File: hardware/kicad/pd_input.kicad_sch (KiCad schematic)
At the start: 46 parts, among them J1 USB-C USB (Power), J14 noknok_Pico_Socket_P1-20, J15 noknok_Pico_Socket_P21-40, J8 SWD pads, U1 CH32X035G8U6, U4 INA180A2, U5 noknok_ME6203A33M3G

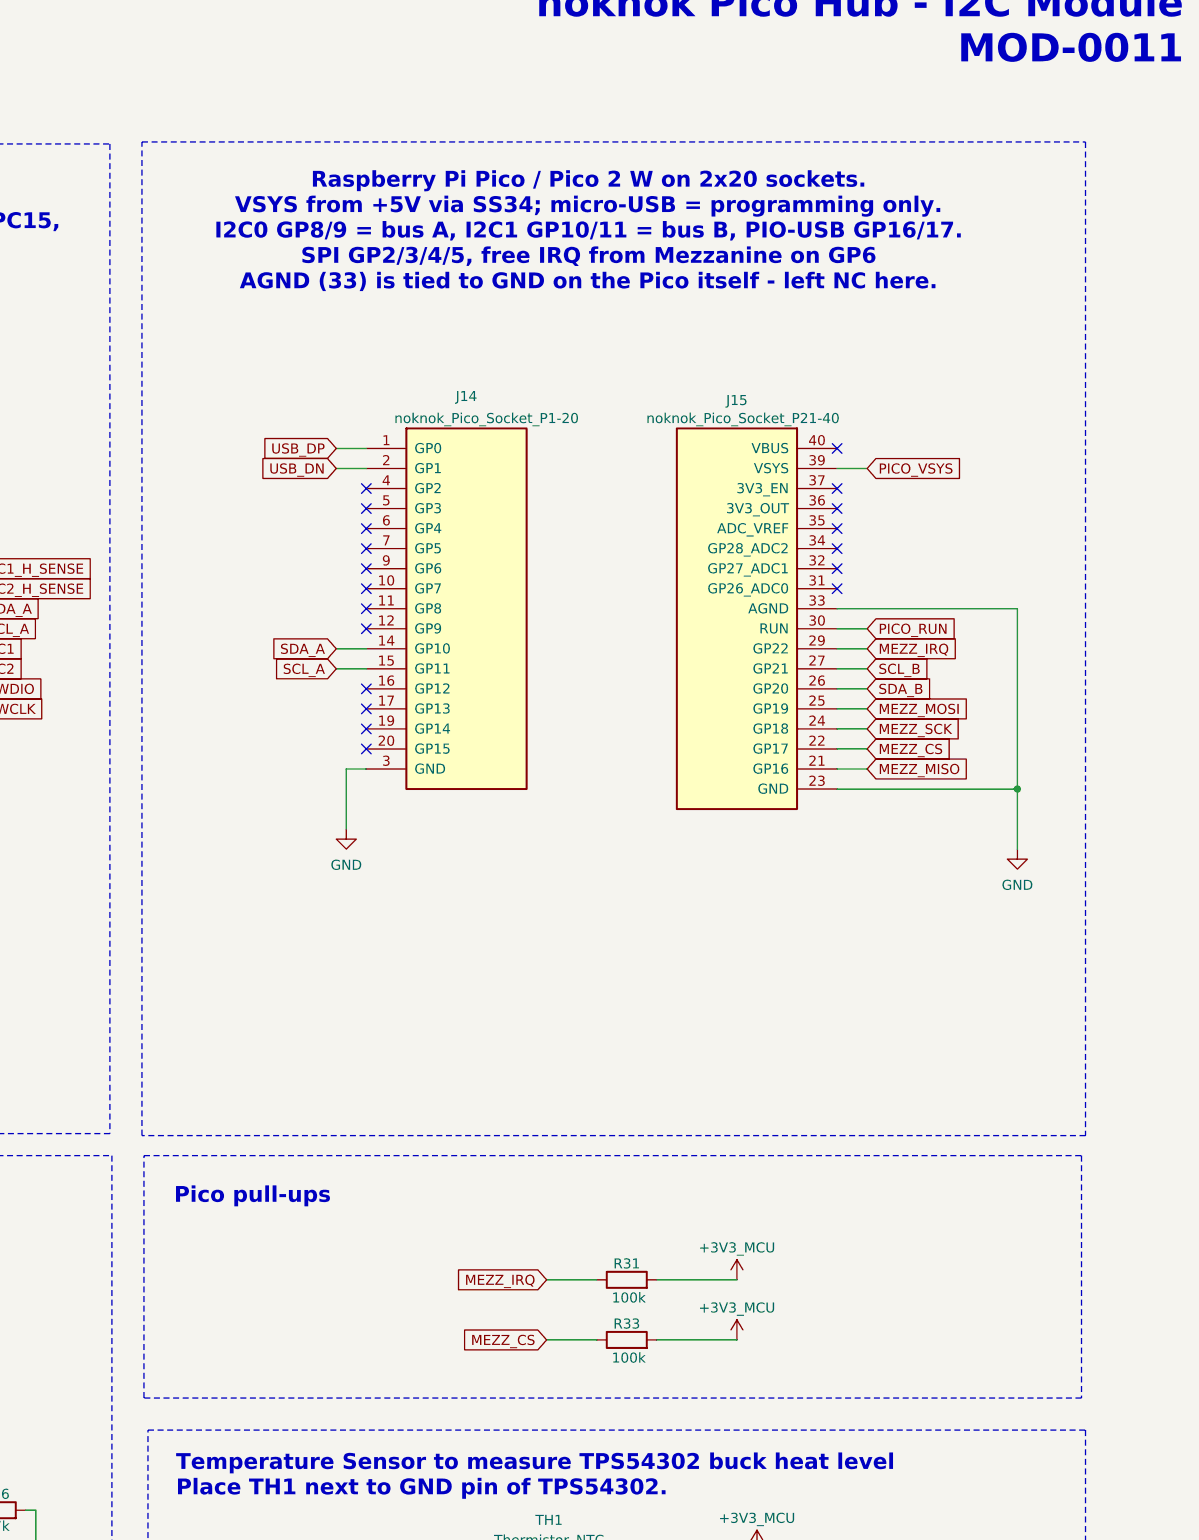
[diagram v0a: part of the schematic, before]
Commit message: DEV-45: rev 1.1 - R39/R40 5.1k pull-downs on USB_DP/USB_DN at the Pico (RP2350 erratum E9), schematic note, layout (D16/D17 shifted 1.75 mm), BOM line 20 now R1,R2,R39,R40 x4 (C23186)
ERC 0. DRC: the 12 known board-edge items only, 0 unconnected, schematic parity 0.
BOM cross-checked against the schematic: 115 parts each.
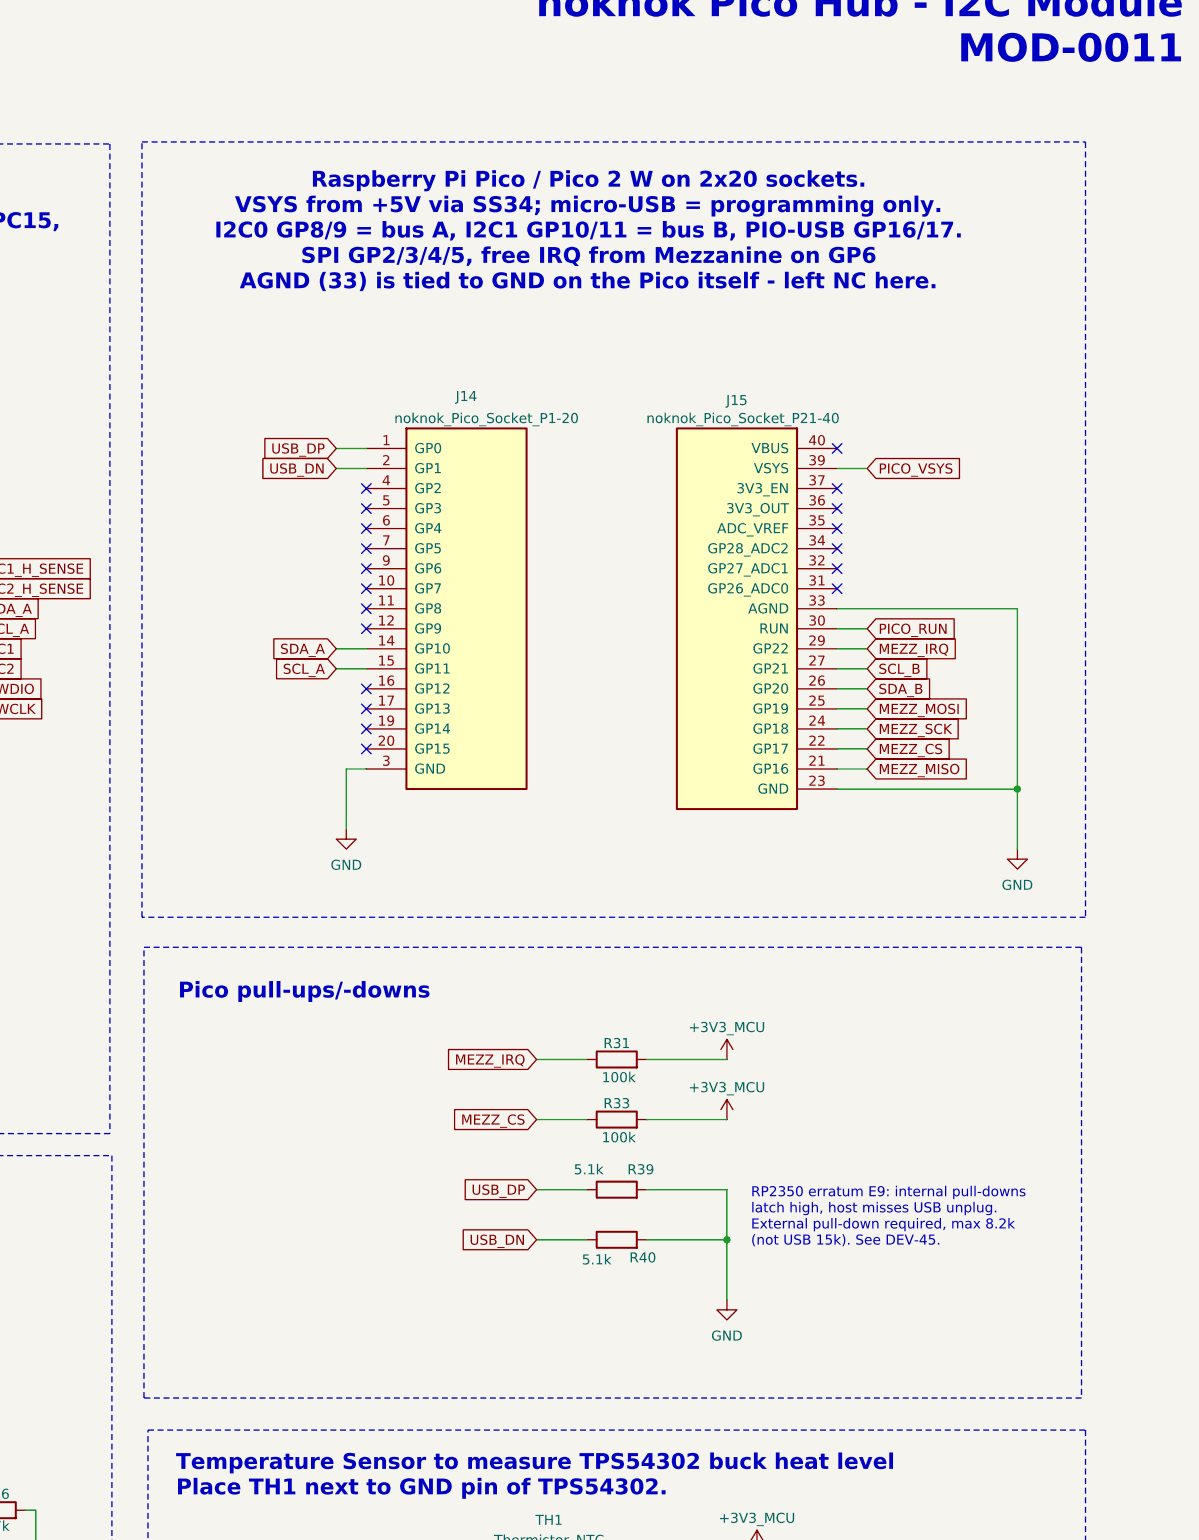
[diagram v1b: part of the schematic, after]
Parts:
- added R39, R40: 5.1k, Resistor_SMD:R_0603_1608Metric, symbol Device:R
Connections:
- net GND: now also R39.2, R40.2
- net USB_DN: now also R40.1
- net USB_DP: now also R39.1
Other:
- note added: "Pico pull-ups/-downs"
- note added: "RP2350 erratum E9: internal pull-downs latch high, host misses USB unplug. External pull-down required, max 8.2k (not USB 15k). See DEV-45."
- note removed: "Pico pull-ups"
- moved on the sheet: R31, R33
